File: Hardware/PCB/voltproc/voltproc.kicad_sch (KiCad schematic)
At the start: 55 parts, among them J1 Synth_power_2x5, J10 Jack, J11 Jack, J12 Jack, J13 Jack, J2 Jack, J4 Jack, J5 Jack, J6 Jack, J7 Jack, J8 Jack, J9 Jack, U1 TL074, U2 TL071

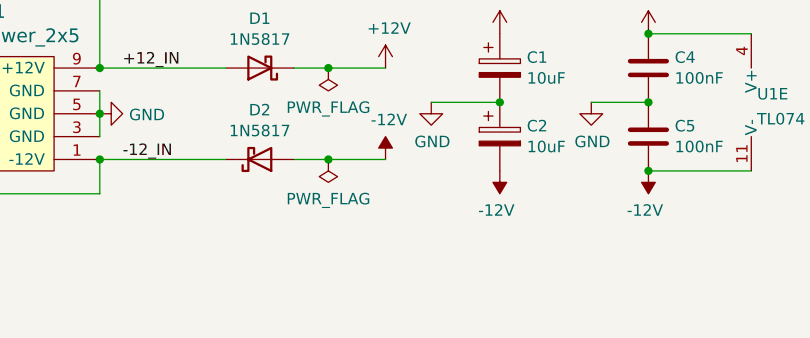
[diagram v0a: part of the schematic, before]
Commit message: Better .gitignore; add test points
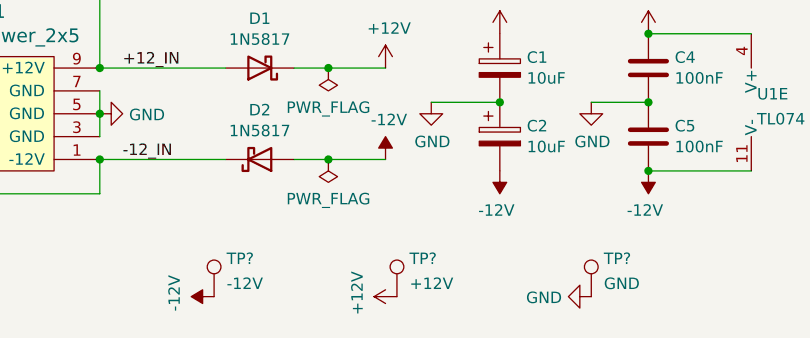
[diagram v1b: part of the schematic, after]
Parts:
- added TP?: -12V, ao_tht:TestPoint_THTPad_D1.5mm_Drill0.7mm, symbol ao_symbols:TestPoint
- added TP?: GND, ao_tht:TestPoint_THTPad_1.5x1.5mm_Drill0.7mm, symbol ao_symbols:TestPoint
- added TP?: +12V, ao_tht:TestPoint_THTPad_D1.5mm_Drill0.7mm, symbol ao_symbols:TestPoint
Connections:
- net +12V: now also TP?.1
- net -12V: now also TP?.1
- net GND: now also TP?.1
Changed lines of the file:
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@@
     (pin "T")
+  )
+  (symbol (lib_id "power:GND") (at 113.03 198.12 270) (unit 1)
+    (in_bom yes) (on_board yes)
+    (property "Reference" "#PWR?" (id 0) (at 106.68 198.12 0)
+      (effects (font (size 1.27 1.27)) hide)
+    )
+    (property "Value" "GND" (id 1) (at 109.7788 198.247 90)
+      (effects (font (size 1.27 1.27)) (justify right))
+    )
+    (property "Footprint" "" (id 2) (at 113.03 198.12 0)
+      (effects (font (size 1.27 1.27)) hide)
+    )
+    (property "Datasheet" "" (id 3) (at 113.03 198.12 0)
+      (effects (font (size 1.27 1.27)) hide)
+    )
+    (pin "1")
+  )
+  (symbol (lib_id "ao_symbols:TestPoint") (at 71.12 198.12 0) (unit 1)
+    (in_bom yes) (on_board yes) (fields_autoplaced)
+    (property "Reference" "TP?" (id 0) (at 72.517 193.9095 0)
+      (effects (font (size 1.27 1.27)) (justify left))
+    )
+    (property "Value" "-12V" (id 1) (at 72.517 196.6846 0)
+      (effects (font (size 1.27 1.27)) (justify left))
+    )
+    (property "Footprint" "ao_tht:TestPoint_THTPad_D1.5mm_Drill0.7mm" (id 2) (at 76.2 198.12 0)
+      (effects (font (size 1.27 1.27)) hide)
+    )
+    (property "Datasheet" "~" (id 3) (at 76.2 198.12 0)
+      (effects (font (size 1.27 1.27)) hide)
+    )
+    (pin "1")
   )
   (symbol (lib_id "ao_symbols:R") (at 186.69 125.73 90) (unit 1)
@@
     (pin "1")
   )
+  (symbol (lib_id "power:-12V") (at 71.12 198.12 90) (unit 1)
+    (in_bom yes) (on_board yes)
+    (property "Reference" "#PWR?" (id 0) (at 68.58 198.12 0)
+      (effects (font (size 1.27 1.27)) hide)
+    )
+    (property "Value" "-12V" (id 1) (at 66.7258 197.739 0))
+    (property "Footprint" "" (id 2) (at 71.12 198.12 0)
+      (effects (font (size 1.27 1.27)) hide)
+    )
+    (property "Datasheet" "" (id 3) (at 71.12 198.12 0)
+      (effects (font (size 1.27 1.27)) hide)
+    )
+    (pin "1")
+  )
   (symbol (lib_id "power:GND") (at 101.6 59.69 0) (unit 1)
     (in_bom yes) (on_board yes) (fields_autoplaced)
@@
     (pin "2")
     (pin "3")
+  )
+  (symbol (lib_id "power:+12V") (at 91.44 198.12 90) (unit 1)
+    (in_bom yes) (on_board yes)
+    (property "Reference" "#PWR?" (id 0) (at 95.25 198.12 0)
+      (effects (font (size 1.27 1.27)) hide)
+    )
+    (property "Value" "+12V" (id 1) (at 87.0458 197.739 0))
+    (property "Footprint" "" (id 2) (at 91.44 198.12 0)
+      (effects (font (size 1.27 1.27)) hide)
+    )
+    (property "Datasheet" "" (id 3) (at 91.44 198.12 0)
+      (effects (font (size 1.27 1.27)) hide)
+    )
+    (pin "1")
   )
   (symbol (lib_id "power:GND") (at 200.66 53.34 0) (mirror y) (unit 1)
@@
     (pin "2")
   )
+  (symbol (lib_id "ao_symbols:TestPoint") (at 113.03 198.12 0) (unit 1)
+    (in_bom yes) (on_board yes) (fields_autoplaced)
+    (property "Reference" "TP?" (id 0) (at 114.427 193.9095 0)
+      (effects (font (size 1.27 1.27)) (justify left))
+    )
+    (property "Value" "GND" (id 1) (at 114.427 196.6846 0)
+      (effects (font (size 1.27 1.27)) (justify left))
+    )
+    (property "Footprint" "ao_tht:TestPoint_THTPad_1.5x1.5mm_Drill0.7mm" (id 2) (at 118.11 198.12 0)
+      (effects (font (size 1.27 1.27)) hide)
+    )
+    (property "Datasheet" "~" (id 3) (at 118.11 198.12 0)
+      (effects (font (size 1.27 1.27)) hide)
+    )
+    (pin "1")
+  )
   (symbol (lib_id "ao_symbols:R") (at 170.18 76.2 90) (unit 1)
     (in_bom yes) (on_board yes)
@@
     (pin "3")
   )
+  (symbol (lib_id "ao_symbols:TestPoint") (at 91.44 198.12 0) (unit 1)
+    (in_bom yes) (on_board yes) (fields_autoplaced)
+    (property "Reference" "TP?" (id 0) (at 92.837 193.9095 0)
+      (effects (font (size 1.27 1.27)) (justify left))
+    )
+    (property "Value" "+12V" (id 1) (at 92.837 196.6846 0)
+      (effects (font (size 1.27 1.27)) (justify left))
+    )
+    (property "Footprint" "ao_tht:TestPoint_THTPad_D1.5mm_Drill0.7mm" (id 2) (at 96.52 198.12 0)
+      (effects (font (size 1.27 1.27)) hide)
+    )
+    (property "Datasheet" "~" (id 3) (at 96.52 198.12 0)
+      (effects (font (size 1.27 1.27)) hide)
+    )
+    (pin "1")
+  )
   (symbol (lib_id "Connector:AudioJack2") (at 207.01 93.98 180) (unit 1)
     (in_bom yes) (on_board yes)
@@
       (reference "#PWR0110") (unit 1) (value "-12V") (footprint "")
     )
+    (path "/18a17eb6-f45e-4c15-bce2-217ce6b1e774"
+      (reference "#PWR?") (unit 1) (value "GND") (footprint "")
+    )
+    (path "/2c831197-3673-4a55-945e-4f3263f57df0"
+      (reference "#PWR?") (unit 1) (value "-12V") (footprint "")
+    )
+    (path "/5032b52d-fb14-4fb1-916e-c43f68350d75"
+      (reference "#PWR?") (unit 1) (value "+12V") (footprint "")
+    )
     (path "/00000000-0000-0000-0000-00005f73fa30"
       (reference "C1") (unit 1) (value "10uF") (footprint "ao_tht:CP_Radial_D6.3mm_P2.50mm")
@@
       (reference "RV4") (unit 1) (value "A1M") (footprint "")
     )
+    (path "/18e9f180-adaa-4063-b433-8c7af5ab470b"
+      (reference "TP?") (unit 1) (value "-12V") (footprint "ao_tht:TestPoint_THTPad_D1.5mm_Drill0.7mm")
+    )
+    (path "/beb27022-33ac-4698-9809-f25d7ef525da"
+      (reference "TP?") (unit 1) (value "GND") (footprint "ao_tht:TestPoint_THTPad_1.5x1.5mm_Drill0.7mm")
+    )
+    (path "/e3425811-e111-437c-8bf3-b2d34027d572"
+      (reference "TP?") (unit 1) (value "+12V") (footprint "ao_tht:TestPoint_THTPad_D1.5mm_Drill0.7mm")
+    )
     (path "/dfd26a0d-34e3-4ab3-8a38-0f87d3949841"

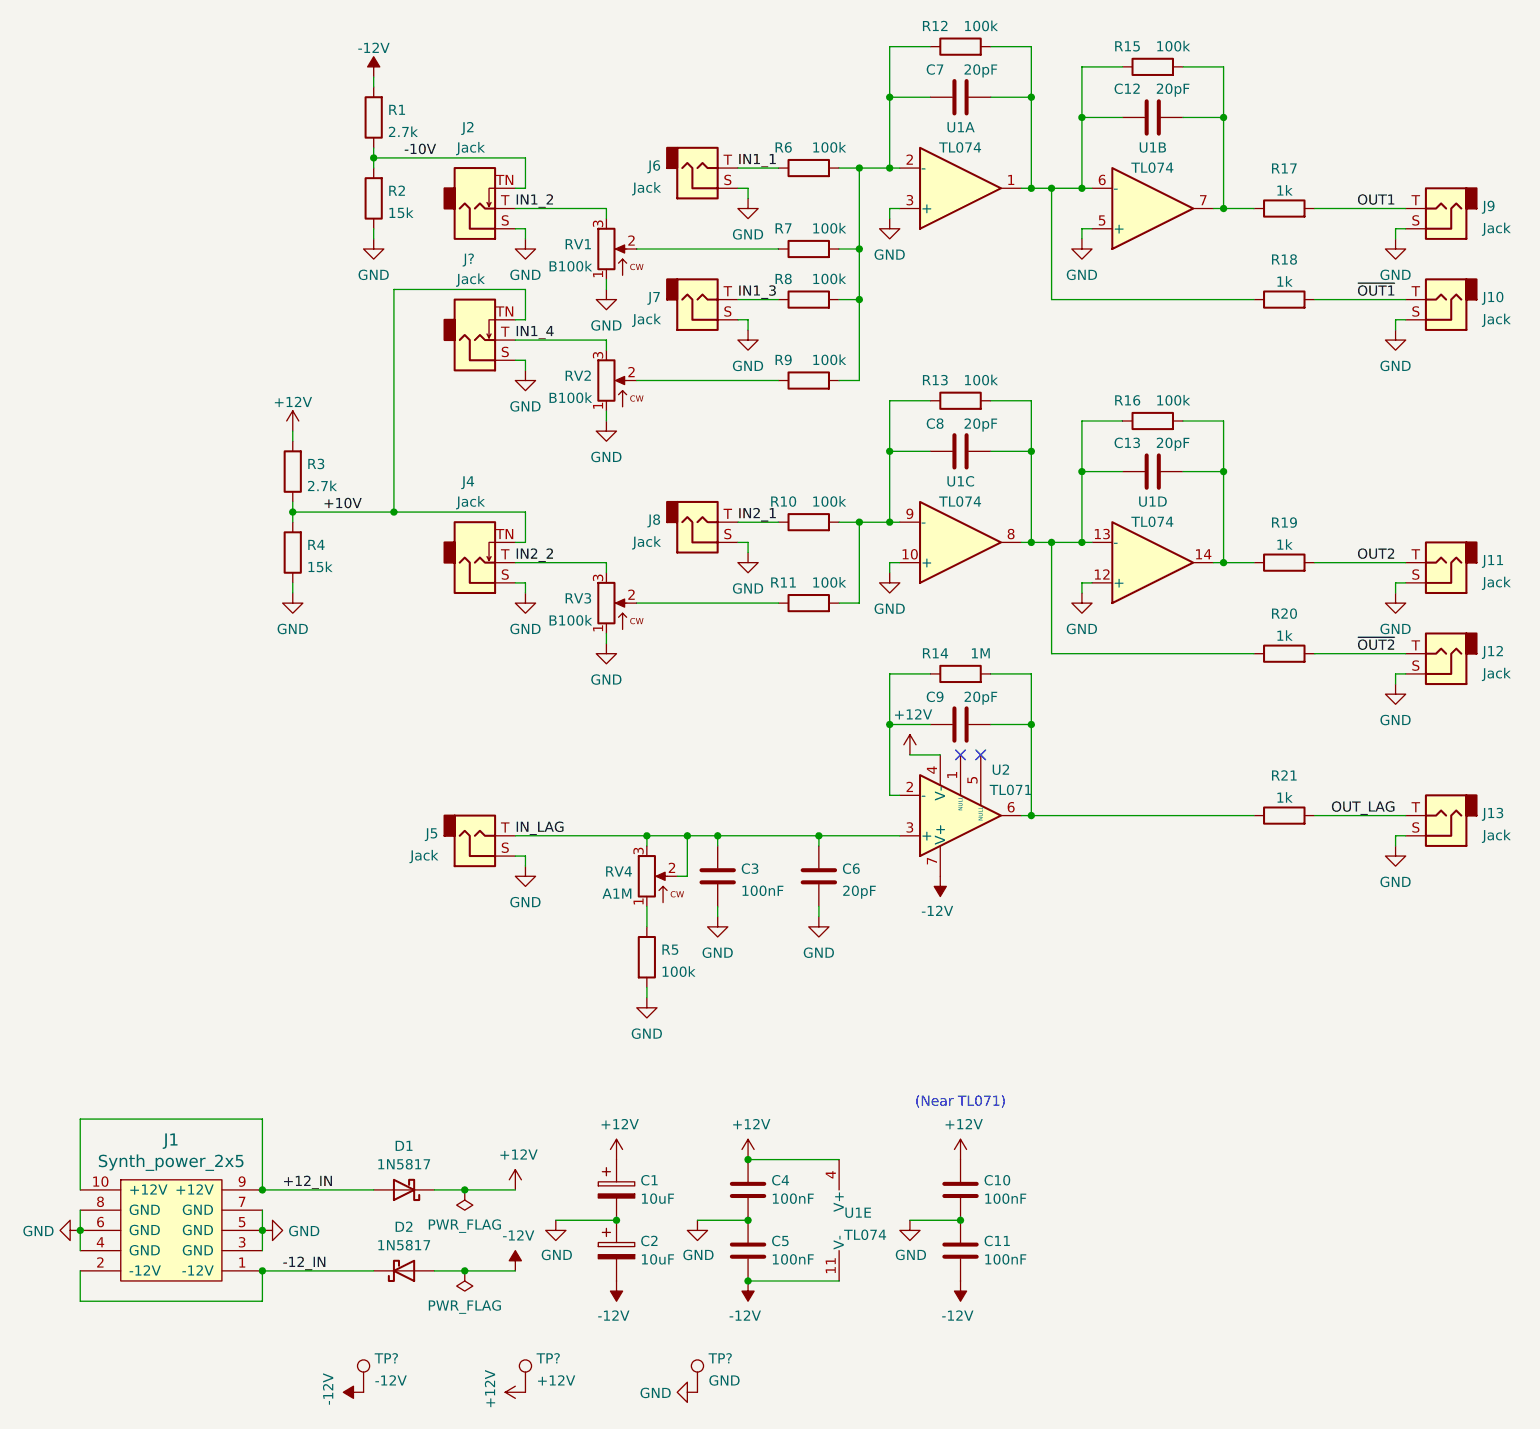
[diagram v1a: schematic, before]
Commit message: reorg schematic, RC and linear lag
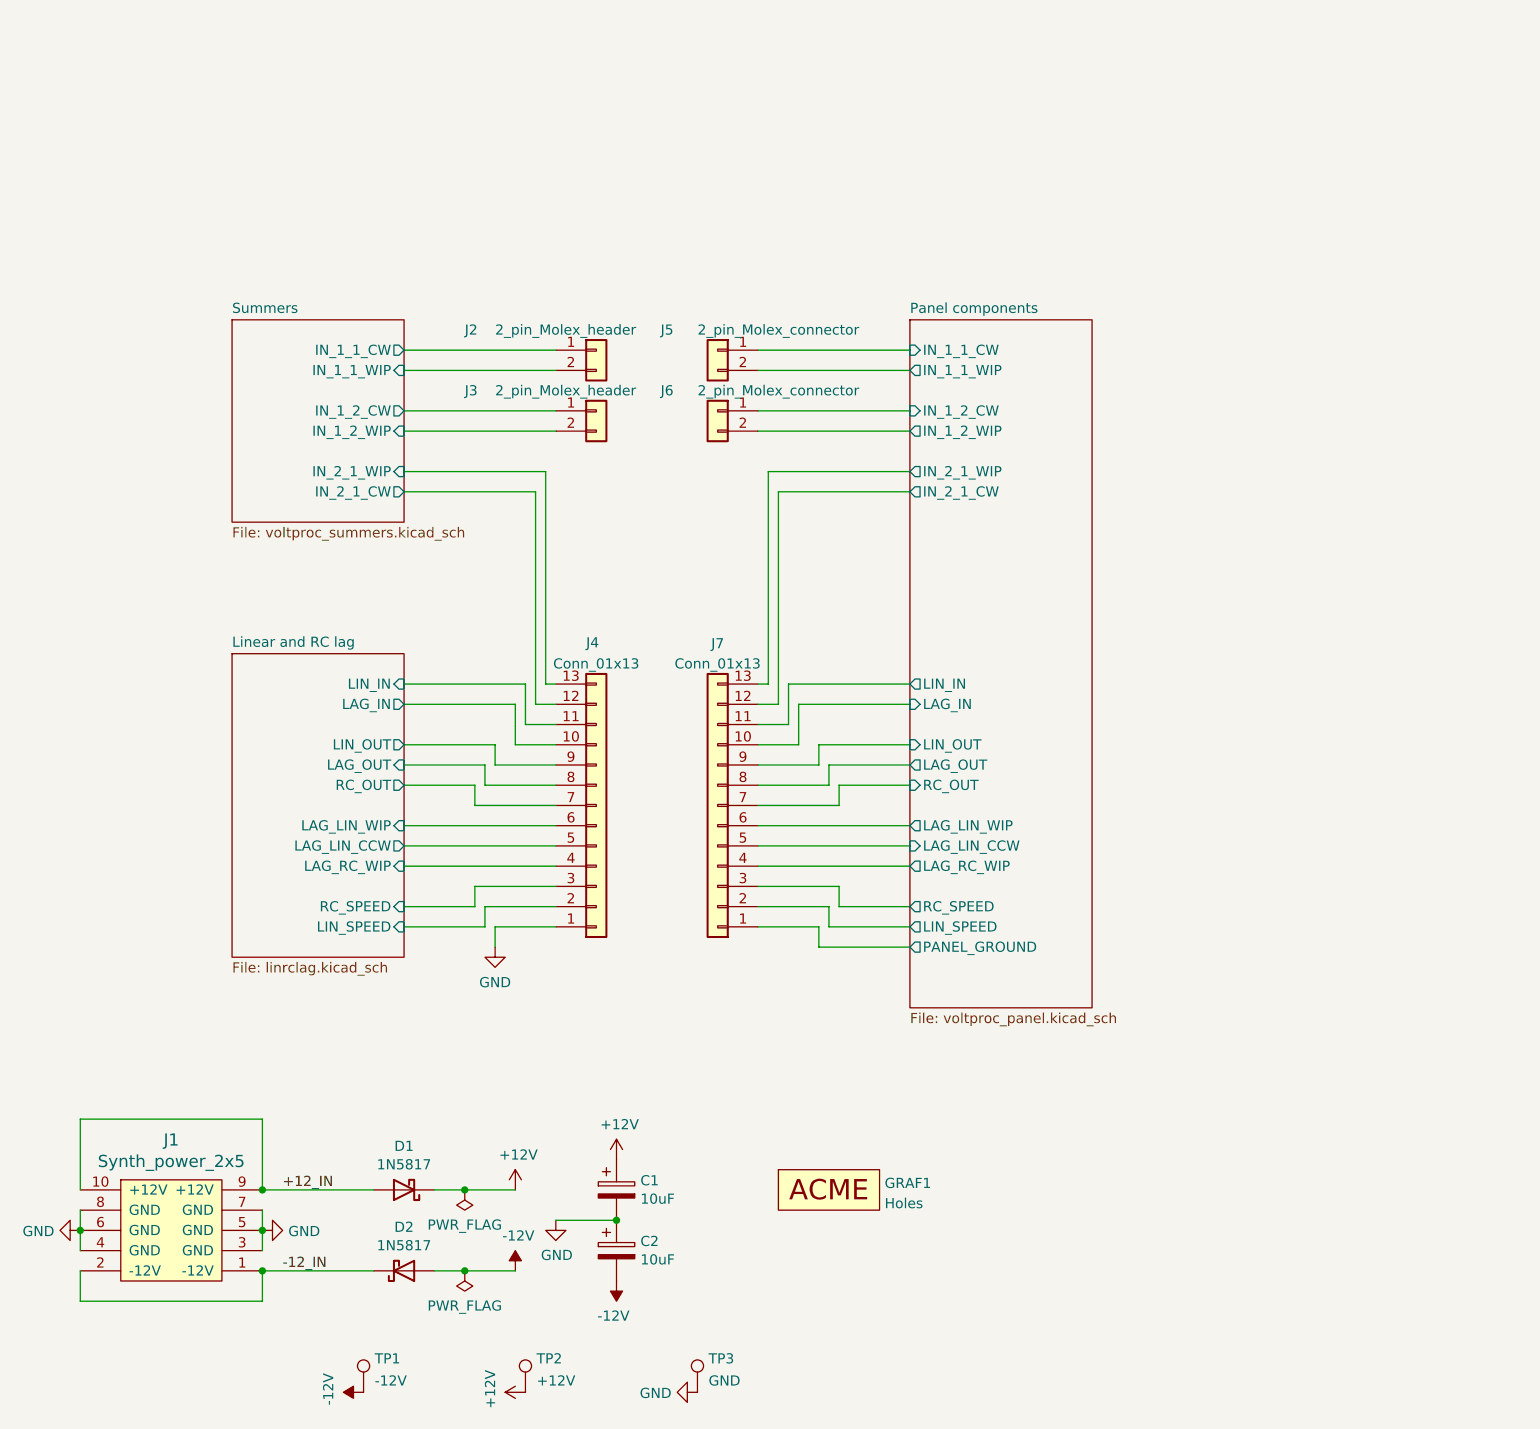
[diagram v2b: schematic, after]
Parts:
- removed C10, C11, C3, C4, C5: 100nF, ao_tht:C_Disc_D3.0mm_W1.6mm_P2.50mm, symbol ao_symbols:C
- removed C12, C13, C6, C7, C8, C9: 20pF, ao_tht:C_Disc_D3.0mm_W1.6mm_P2.50mm, symbol ao_symbols:C
- removed J10, J11, J12, J13, J5, J6, J7, J8, J9: Jack, symbol Connector:AudioJack2
- removed J2, J4, J?: Jack, symbol Connector:AudioJack2_SwitchT
- removed R1, R3: 2.7k, ao_tht:R_Axial_DIN0207_L6.3mm_D2.5mm_P10.16mm_Horizontal, symbol ao_symbols:R
- removed R10, R11, R12, R13, R15, R16, R5, R6, R7, R8, R9: 100k, ao_tht:R_Axial_DIN0207_L6.3mm_D2.5mm_P10.16mm_Horizontal, symbol ao_symbols:R
- removed R14: 1M, ao_tht:R_Axial_DIN0207_L6.3mm_D2.5mm_P10.16mm_Horizontal, symbol ao_symbols:R
- removed R17, R18, R19, R20, R21: 1k, ao_tht:R_Axial_DIN0207_L6.3mm_D2.5mm_P10.16mm_Horizontal, symbol ao_symbols:R
- removed R2, R4: 15k, ao_tht:R_Axial_DIN0207_L6.3mm_D2.5mm_P10.16mm_Horizontal, symbol ao_symbols:R
- removed RV1, RV2, RV3: B100k, symbol ao_symbols:R_POT
- removed RV4: A1M, symbol ao_symbols:R_POT
- removed U1: TL074, symbol Amplifier_Operational:TL074
- removed U2: TL071, ao_tht:DIP-8_W7.62mm_Socket_LongPads, symbol ao_symbols:TL071
- added GRAF1: Holes, voltproc:voltproc_panel_holes, symbol ao_symbols:Graphic
- added J2, J3: 2_pin_Molex_header, ao_tht:Molex_KK-254_AE-6410-02A_1x02_P2.54mm_Vertical, symbol ao_symbols:2_pin_Molex_header
- added J4: Conn_01x13, Connector_PinHeader_2.54mm:PinHeader_1x13_P2.54mm_Vertical, symbol Connector_Generic:Conn_01x13
- added J5, J6: 2_pin_Molex_connector, ao_tht:Molex_KK-254_AE-6410-02A_1x02_P2.54mm_Vertical, symbol ao_symbols:2_pin_Molex_connector
- added J7: Conn_01x13, Connector_PinSocket_2.54mm:PinSocket_1x13_P2.54mm_Vertical, symbol Connector_Generic:Conn_01x13
- gave numbers to parts that had none: 3
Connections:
- net GND: now also J4.1 (Pin_1)
- new net Linear and RC lag/LAG_IN: J4.10 (Pin_10)
- new net Linear and RC lag/LAG_LIN_CCW: J4.5 (Pin_5)
- new net Linear and RC lag/LAG_LIN_WIP: J4.6 (Pin_6)
- new net Linear and RC lag/LAG_OUT: J4.8 (Pin_8)
- new net Linear and RC lag/LAG_RC_WIP: J4.4 (Pin_4)
- new net Linear and RC lag/LIN_IN: J4.11 (Pin_11)
- new net Linear and RC lag/LIN_OUT: J4.9 (Pin_9)
- new net Linear and RC lag/LIN_SPEED: J4.2 (Pin_2)
- new net Linear and RC lag/RC_OUT: J4.7 (Pin_7)
- new net Linear and RC lag/RC_SPEED: J4.3 (Pin_3)
- new net Panel components/IN_1_1_CW: J5.1 (Pin_1)
- new net Panel components/IN_1_1_WIP: J5.2 (Pin_2)
- new net Panel components/IN_1_2_CW: J6.1 (Pin_1)
- new net Panel components/IN_1_2_WIP: J6.2 (Pin_2)
- new net Panel components/IN_2_1_CW: J7.12 (Pin_12)
- new net Panel components/IN_2_1_WIP: J7.13 (Pin_13)
- new net Panel components/LAG_IN: J7.10 (Pin_10)
- new net Panel components/LAG_LIN_CCW: J7.5 (Pin_5)
- new net Panel components/LAG_LIN_WIP: J7.6 (Pin_6)
- new net Panel components/LAG_OUT: J7.8 (Pin_8)
- new net Panel components/LAG_RC_WIP: J7.4 (Pin_4)
- new net Panel components/LIN_IN: J7.11 (Pin_11)
- new net Panel components/LIN_OUT: J7.9 (Pin_9)
- new net Panel components/LIN_SPEED: J7.2 (Pin_2)
- new net Panel components/PANEL_GROUND: J7.1 (Pin_1)
- new net Panel components/RC_OUT: J7.7 (Pin_7)
- new net Panel components/RC_SPEED: J7.3 (Pin_3)
- new net Summers/IN_1_1_CW: J2.1 (Pin_1)
- new net Summers/IN_1_1_WIP: J2.2 (Pin_2)
- new net Summers/IN_1_2_CW: J3.1 (Pin_1)
- new net Summers/IN_1_2_WIP: J3.2 (Pin_2)
- new net Summers/IN_2_1_CW: J4.12 (Pin_12)
- new net Summers/IN_2_1_WIP: J4.13 (Pin_13)
- no-connect marks 2 -> 0
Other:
- added sheet Linear and RC lag (linrclag.kicad_sch)
- added sheet Panel components (voltproc_panel.kicad_sch)
- added sheet Summers (voltproc_summers.kicad_sch)
- note removed: "(Near TL071)"
